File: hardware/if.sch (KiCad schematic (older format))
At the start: 59 parts, among them U34 ADA4940-2, U35 ADA4940-2

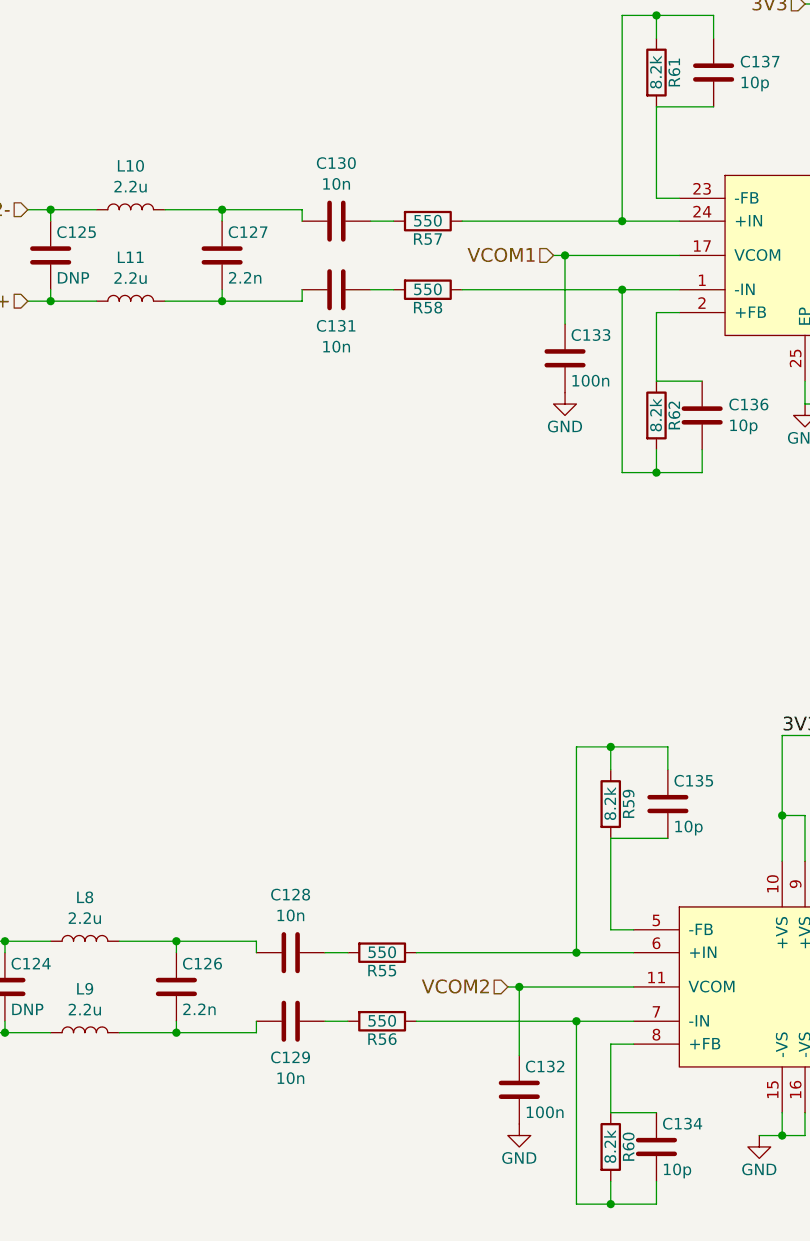
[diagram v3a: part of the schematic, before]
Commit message: Added MFNs to components.
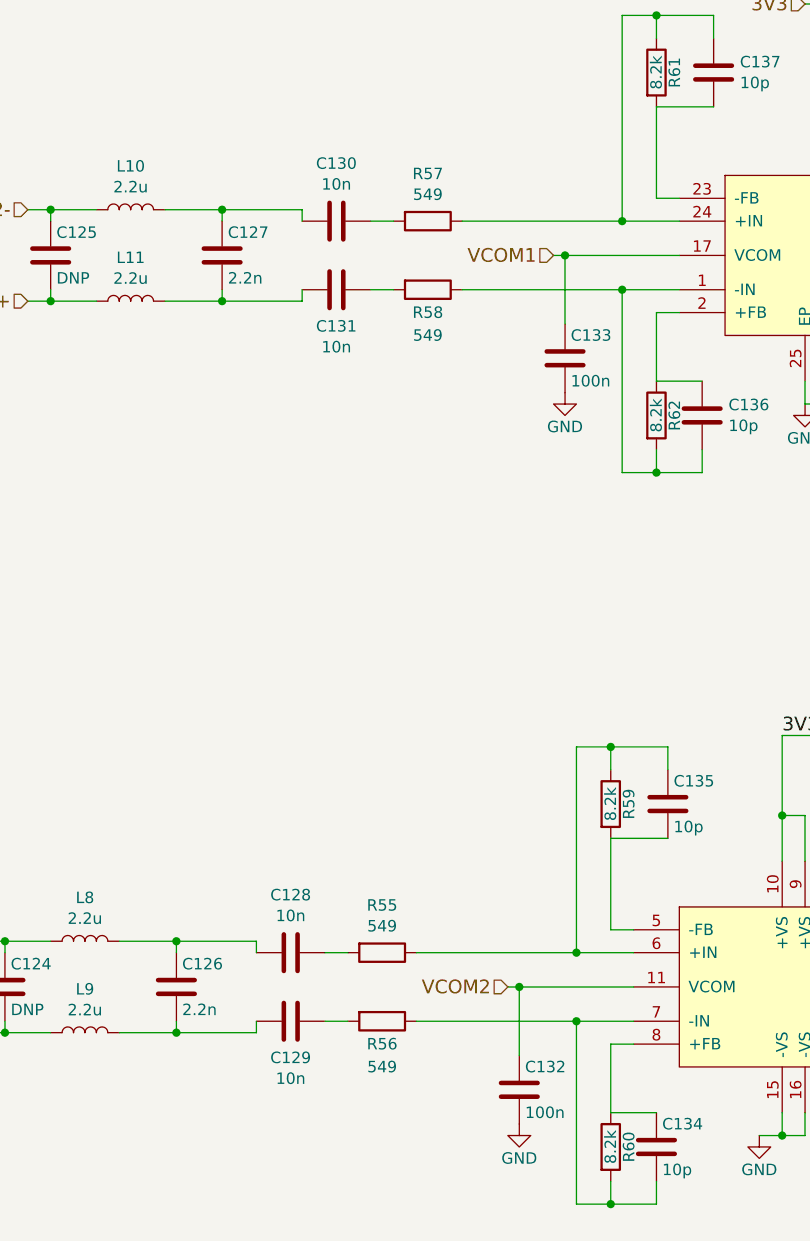
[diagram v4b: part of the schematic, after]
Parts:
- C126, C127: MFN (none) -> CL05B223KP5NNNC
- C128, C129, C130, C131: MFN (none) -> GRM155R71E103KA01D
- C132, C133, C138, C139, C150, C151: MFN (none) -> CL05B104KO5NNNC
- C134, C135, C136, C137: MFN (none) -> GRM1555C1H100FA01D
- L10, L11, L8, L9: footprint fmcw:C_0805b -> Inductor_SMD:L_0805_2012Metric; MFN (none) -> LQM21PN2R2MC0D
- R55, R56, R57, R58: value 550 -> 549; footprint fmcw:R_0402b -> Resistor_SMD:R_0402_1005Metric; MFN (none) -> ERJ-2RKF5490X
- R59, R60, R61, R62: footprint fmcw:R_0402b -> Resistor_SMD:R_0402_1005Metric; MFN (none) -> ERJ-2RKF8201X
- R63, R64, R65, R66, R67, R68, R74, R75, R76, R77, R78, R86: footprint fmcw:R_0402b -> Resistor_SMD:R_0402_1005Metric
- R87, R89, R90, R94: footprint fmcw:R_0402b -> Resistor_SMD:R_0402_1005Metric; MFN (none) -> ERJ-2GE0R00X
- U34, U35: footprint fmcw:VFQFN-24 -> Package_DFN_QFN:WQFN-24-1EP_4x4mm_P0.5mm_EP2.7x2.7mm; MFN (none) -> ADA4940-2ACPZ-R2

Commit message: Improved documentation and added schematics to default libraries.
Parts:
- removed U34: ADA4940-2, Package_DFN_QFN:WQFN-24-1EP_4x4mm_P0.5mm_EP2.7x2.7mm, symbol fmcw-rescue:ADA4940-2-fmcw3-rescue
- added U33: ADA4940-2, Package_CSP:LFCSP-WQ-24-7EP_4x4mm_P0.5mm_EP2.6416x2.6416mm, symbol Amplifier_Difference:ADA4940-2
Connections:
- net labels added: VOCM1, VOCM2
- net labels removed: VCOM1, VCOM2
- wire segments 217 -> 213
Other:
- moved on the sheet: C128, C129, C130, C131, C132, C133, C134, C135, C138, L10, L11, L8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

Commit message: Improved tx sheet and corresponding documentation.
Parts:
- U33: symbol Amplifier_Difference:ADA4940-2 -> fmcw-rescue:ADA4940-2-Amplifier_Difference
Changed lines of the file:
@@
 3V3
 $Comp
-L Amplifier_Difference:ADA4940-2 U33
+L fmcw-rescue:ADA4940-2-Amplifier_Difference U33
 U 1 1 5C3DAB96
 P 4650 1900
@@
 	3900 2350 3900 2450
 $Comp
-L Amplifier_Difference:ADA4940-2 U33
+L fmcw-rescue:ADA4940-2-Amplifier_Difference U33
 U 2 1 5C5E7E6D
 P 4650 5100
@@
 	3400 2000 3250 2000
 $Comp
-L power:GND #PWR?
+L power:GND #PWR0218
 U 1 1 5C886507
 P 3400 2650
-F 0 "#PWR?" H 3400 2400 50  0001 C CNN
+F 0 "#PWR0218" H 3400 2400 50  0001 C CNN
 F 1 "GND" H 3405 2477 50  0000 C CNN
 F 2 "" H 3400 2650 50  0001 C CNN
@@
 	3400 5200 3200 5200
 $Comp
-L power:GND #PWR?
+L power:GND #PWR0220
 U 1 1 5C8DD1D3
 P 3400 5850
-F 0 "#PWR?" H 3400 5600 50  0001 C CNN
+F 0 "#PWR0220" H 3400 5600 50  0001 C CNN
 F 1 "GND" H 3405 5677 50  0000 C CNN
 F 2 "" H 3400 5850 50  0001 C CNN

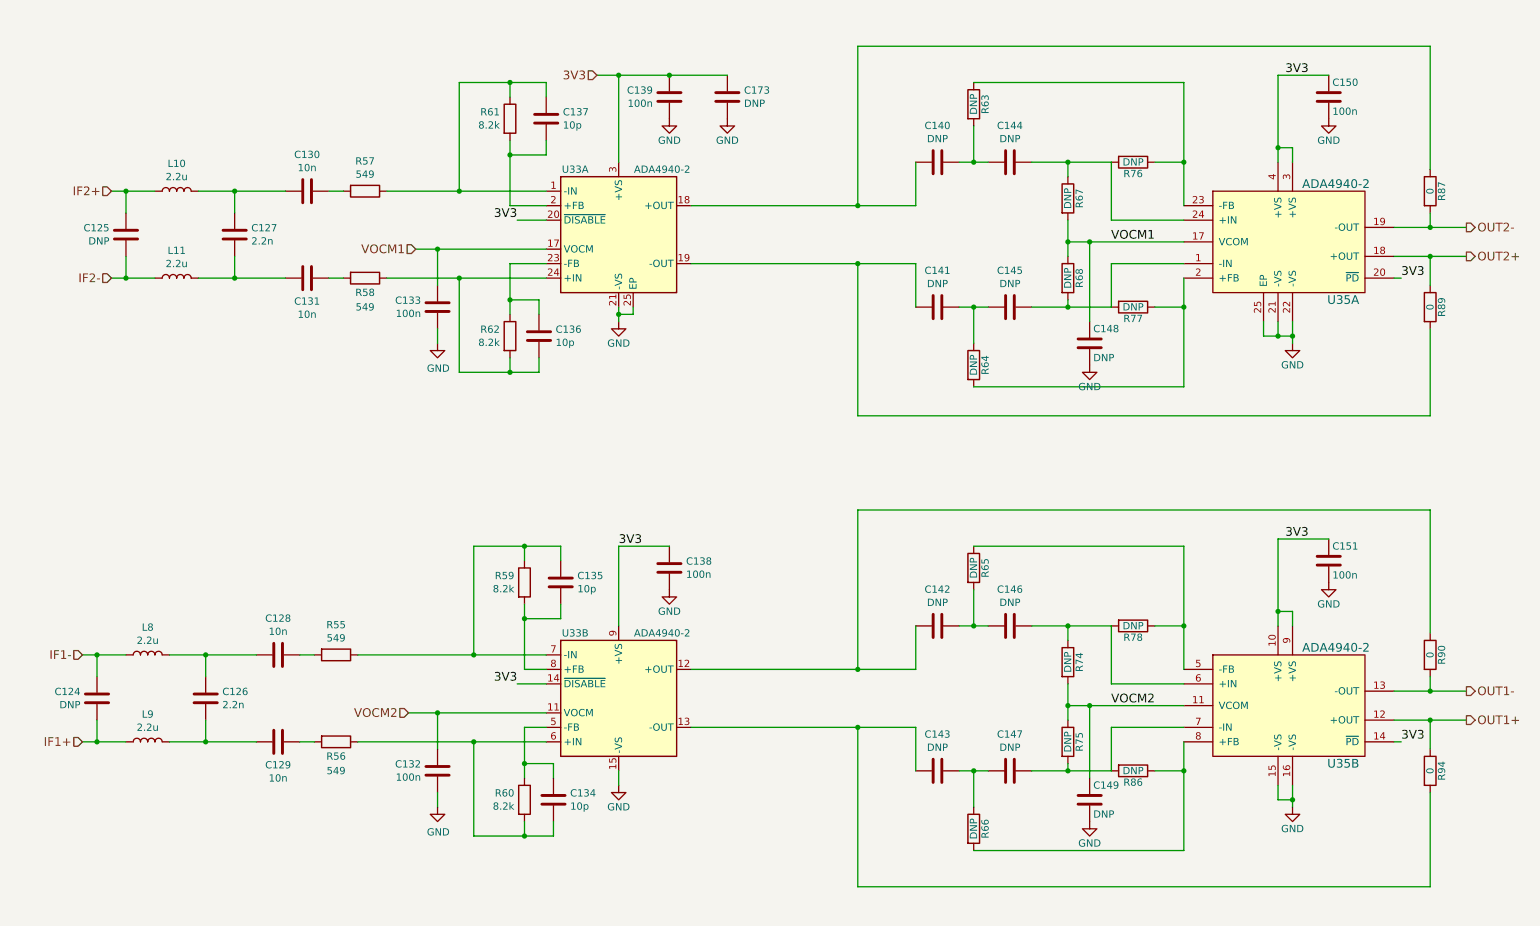
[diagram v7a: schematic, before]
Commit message: Improved documentation and parts of the schematic.
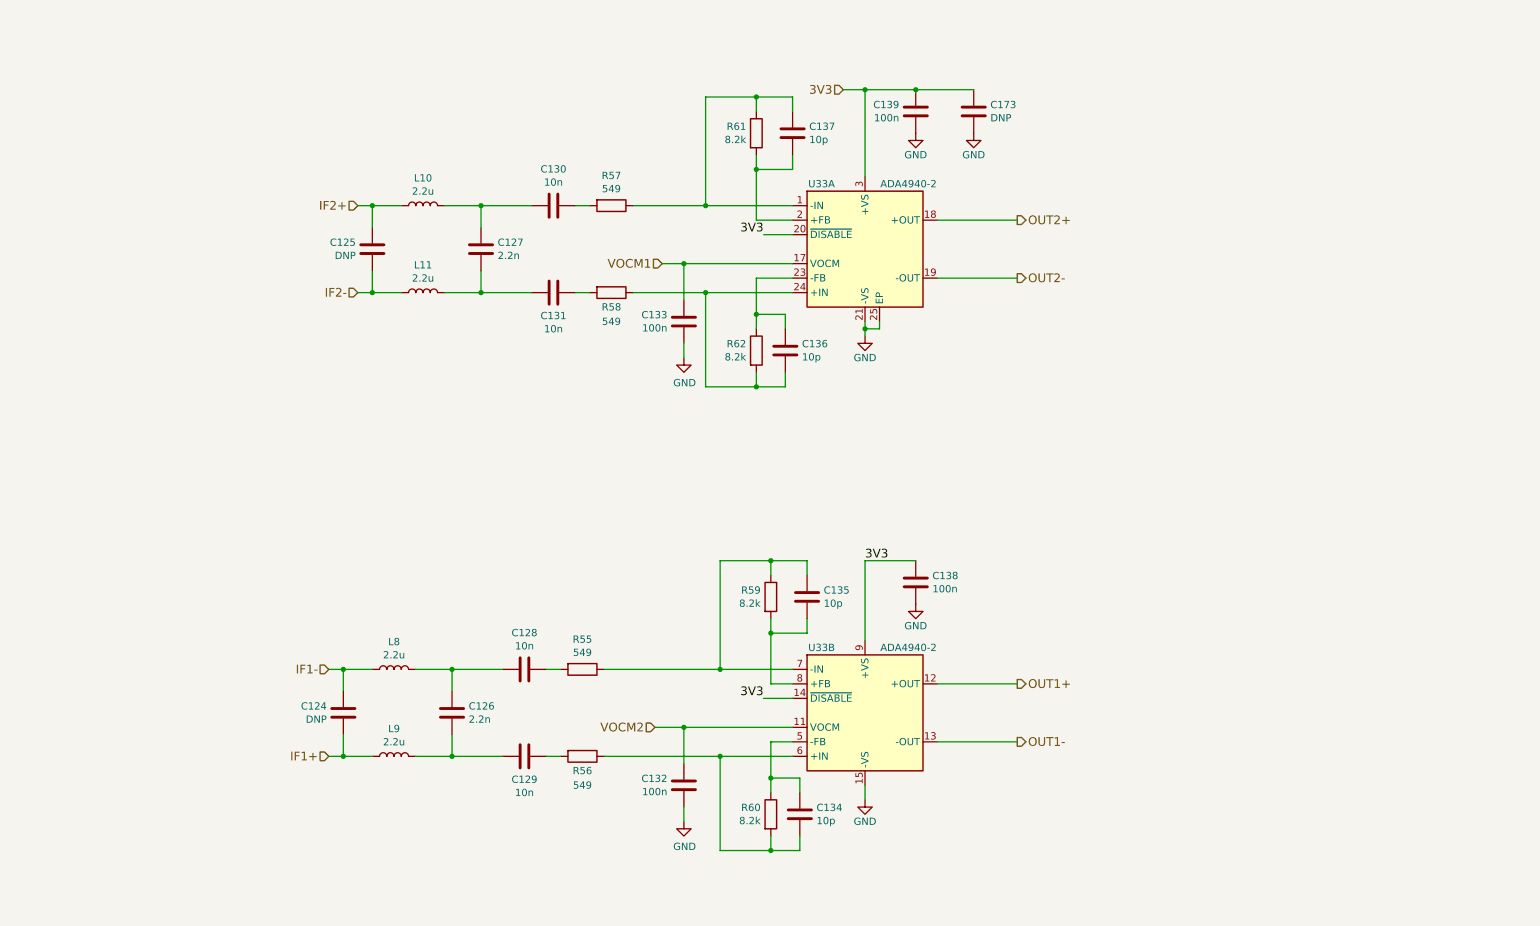
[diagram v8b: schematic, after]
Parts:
- removed C140, C141, C142, C143, C144, C145, C146, C147, C148, C149: DNP, Capacitor_SMD:C_0402_1005Metric, symbol Device:C
- removed C150, C151: 100n, Capacitor_SMD:C_0402_1005Metric, symbol Device:C
- removed R63, R64, R65, R66, R67, R68, R74, R75, R76, R77, R78, R86: DNP, Resistor_SMD:R_0402_1005Metric, symbol Device:R
- removed R87, R89, R90, R94: 0, Resistor_SMD:R_0402_1005Metric, symbol Device:R
- removed U35: ADA4940-2, Package_DFN_QFN:WQFN-24-1EP_4x4mm_P0.5mm_EP2.7x2.7mm, symbol fmcw-rescue:ADA4940-2-fmcw3-rescue
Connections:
- net OUT1+: now also U33.12 (+OUT)
- net OUT1-: now also U33.13 (-OUT)
- net OUT2+: now also U33.18 (+OUT)
- net OUT2-: now also U33.19 (-OUT)
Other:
- moved on the sheet: C124, C125, C126, C127, C128, C129, C130, C131, C132, C133, C134, C135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
